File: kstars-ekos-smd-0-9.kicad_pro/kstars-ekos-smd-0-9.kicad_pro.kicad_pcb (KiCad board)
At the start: 2 copper layers, 86.5 x 56.5 mm, 36 parts, among them J1 Raspberry_Pi_2_3, J2 Conn_01x04, J3 Conn_01x04, U1 AP64501SP-13, U2 TLP3553ATP1_F, U3 TLP3553ATP1_F, U4 TLP3553ATP1_F, U5 TLP3553ATP1_F, U6 TLP241ATP1_F, U7 TLP241ATP1_F

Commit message: Final design submitted to fab.
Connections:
- H5 pad 1: Net-(H5-Pad1) -> GND
- H5 pad 2: GND -> Net-(H5-Pad2)
- U5 pad 4: Net-(H5-Pad1) -> Net-(H5-Pad2)
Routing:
- net Net-(H5-Pad1): track 5.57 -> 0.00 mm, vias 1 -> 0
- net Net-(H5-Pad2): track 0.00 -> 5.45 mm, vias 0 -> 1
- net Net-(C13-Positive): track 32.1 -> 32.9 mm
- net GND: vias 97 -> 98
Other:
- outline, holes or cut-outs redrawn

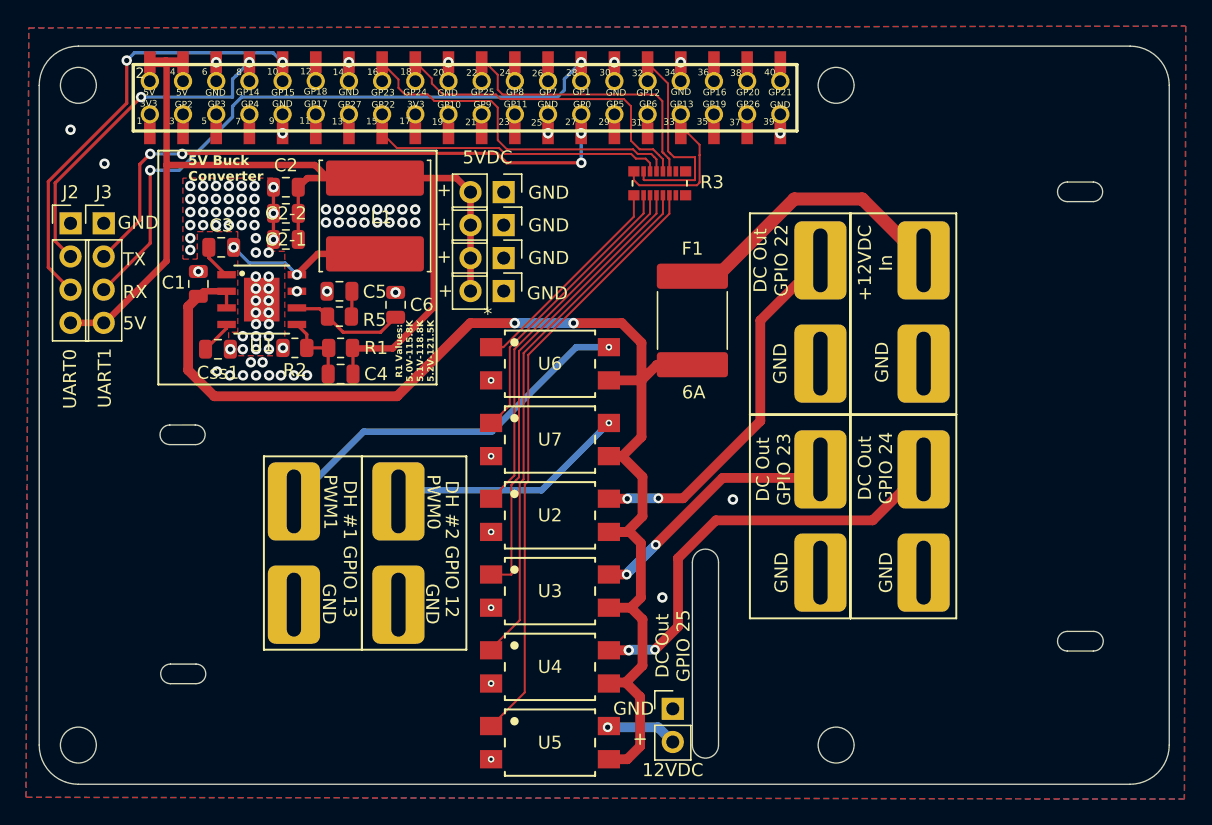
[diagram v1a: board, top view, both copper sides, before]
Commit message: Corrected hole locations.  Final upload to fab.
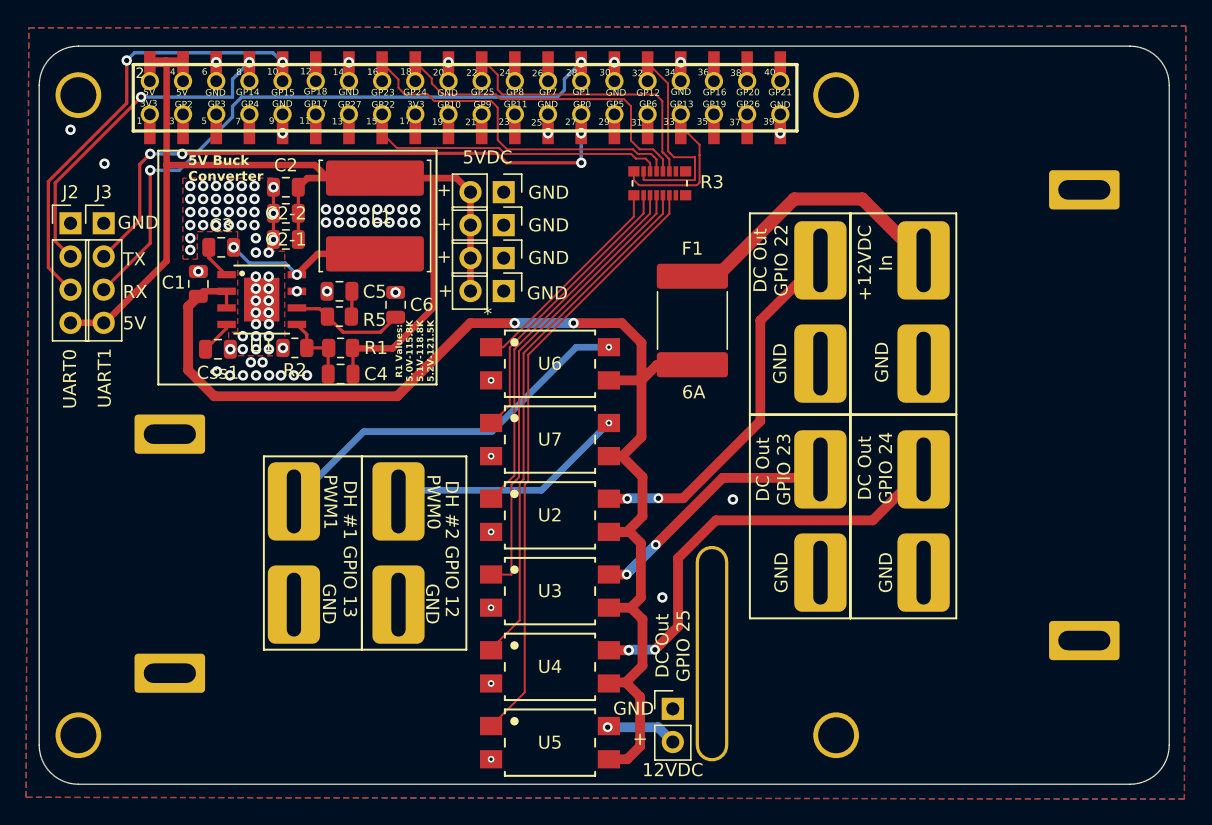
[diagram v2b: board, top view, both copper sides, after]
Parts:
- added REF**: MountingHole_2.75mm_Pad, Mounting_Holes:MountingHole_2.75mm_Pad, F.Cu at (143.0, 79.2)
- added REF**: MountingHole_2.75mm_Pad, Mounting_Holes:MountingHole_2.75mm_Pad, F.Cu at (201.0, 128.2)
- added REF**: Zip_Tie_Hole_1.5mm_2mm_Pad, Mounting_Holes:Zip_Tie_Hole_1.5mm_2mm_Pad, F.Cu at (220.0, 121.0)
- added REF**: Zip_Tie_Hole_1.5mm_2mm_Pad, Mounting_Holes:Zip_Tie_Hole_1.5mm_2mm_Pad, F.Cu at (220.0, 86.5)
- added REF**: Zip_Tie_Hole_1.5mm_2mm_Pad, Mounting_Holes:Zip_Tie_Hole_1.5mm_2mm_Pad, F.Cu at (150.0, 123.5)
- added REF**: Camera_Cable_Hole_2mm_16mm_Pad, Mounting_Holes:Camera_Cable_Hole_2mm_16mm_Pad, F.Cu at (191.5, 122.0)
- added REF**: MountingHole_2.75mm_Pad, Mounting_Holes:MountingHole_2.75mm_Pad, F.Cu at (201.0, 79.2)
- added REF**: Zip_Tie_Hole_1.5mm_2mm_Pad, Mounting_Holes:Zip_Tie_Hole_1.5mm_2mm_Pad, F.Cu at (150.0, 105.2)
- added REF**: MountingHole_2.75mm_Pad, Mounting_Holes:MountingHole_2.75mm_Pad, F.Cu at (143.0, 128.2)
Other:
- outline, holes or cut-outs redrawn

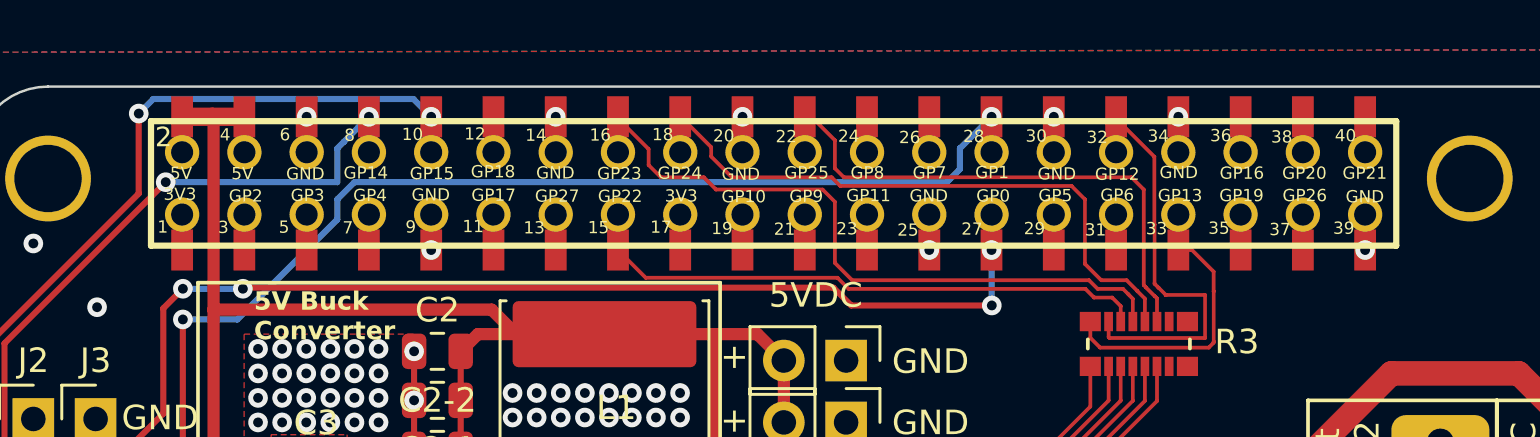
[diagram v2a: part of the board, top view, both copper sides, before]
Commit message: Updated 40-pin numbering silkscreen.
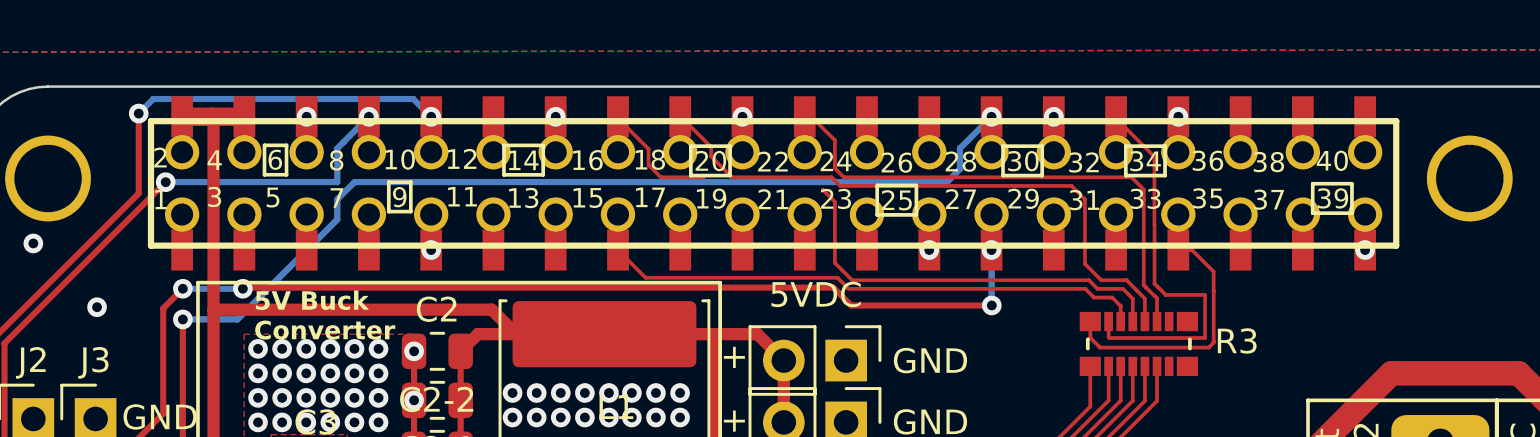
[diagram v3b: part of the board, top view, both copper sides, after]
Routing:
- net DC_2: track 26.8 -> 21.7 mm

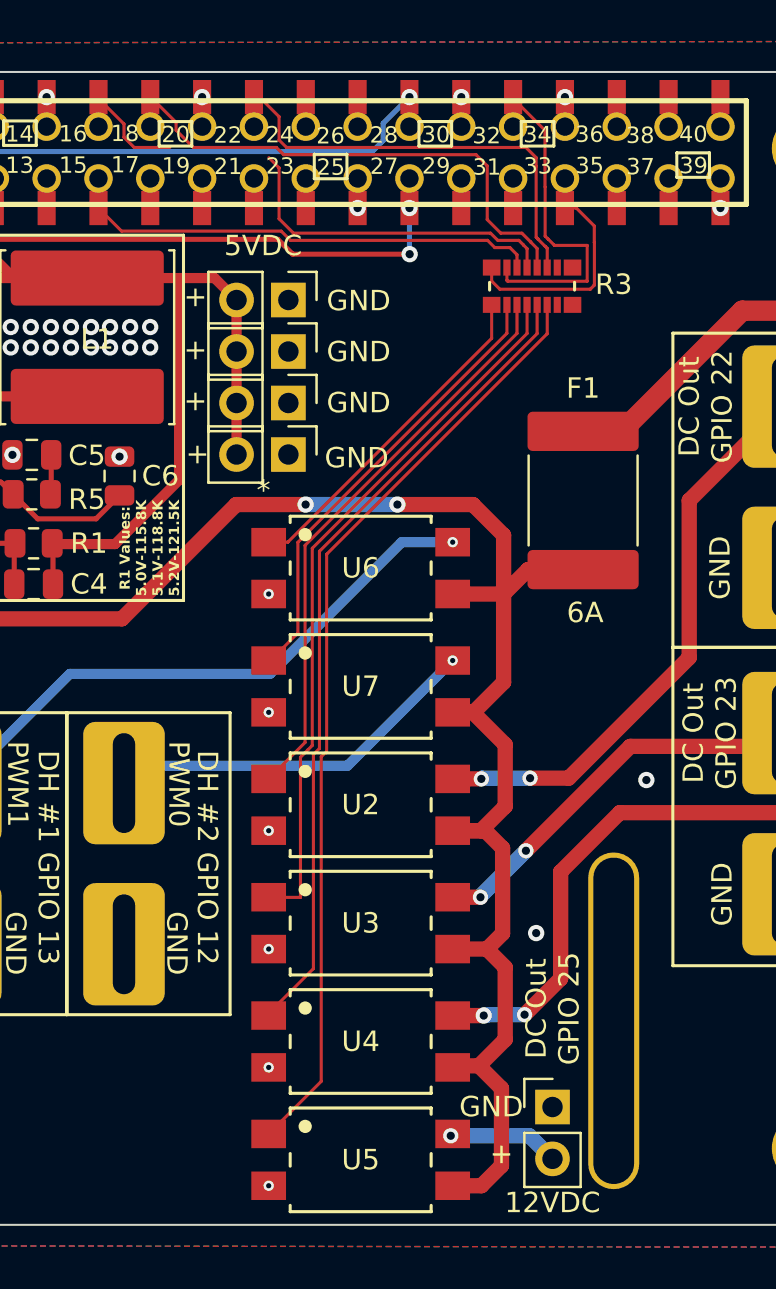
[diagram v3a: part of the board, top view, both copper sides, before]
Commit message: Fixed GPIO16 trace . .
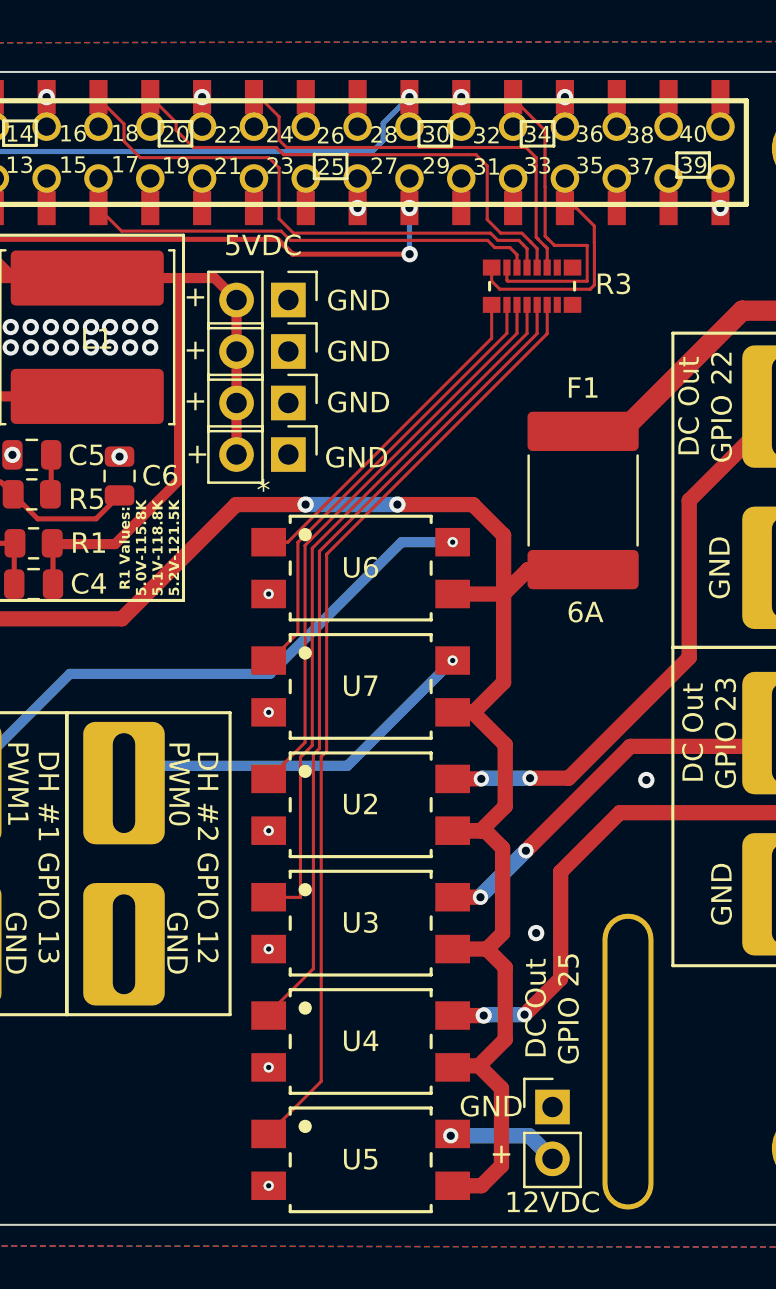
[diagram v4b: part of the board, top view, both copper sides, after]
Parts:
- moved REF** 2.12 mm to (192.2, 124.0)
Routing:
- net DC_2: track 21.7 -> 26.9 mm
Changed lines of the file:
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@@
 	(footprint "Mounting_Holes:Camera_Cable_Hole_2mm_16mm_Pad"
 		(layer "F.Cu")
-		(at 191.5 122 90)
+		(at 192.2 124 90)
 		(descr "Mounting Hole 2.7mm, generated by kicad-footprint-generator mountinghole.py")
 		(tags "mountinghole")
@@
 		(pad "1" thru_hole oval
 			(at 0 0 90)
-			(size 16.5 2.5)
-			(drill oval 16 2)
+			(size 14.5 2.5)
+			(drill oval 14 2)
 			(layers "*.Cu" "*.Mask")
 			(remove_unused_layers yes)
@@
 	)
 	(segment
-		(start 185.9651 83.4)
-		(end 187 83.4)
+		(start 184.7534 79.5534)
+		(end 185.3 80.1)
 		(width 0.1524)
 		(layer "F.Cu")
@@
 	)
 	(segment
-		(start 175.319617 79.5534)
-		(end 184.7534 79.5534)
+		(start 187.43321 83.838058)
+		(end 187.746634 84.15148)
 		(width 0.1524)
 		(layer "F.Cu")
@@
 	)
 	(segment
-		(start 187.43321 83.83321)
-		(end 187.43321 83.838058)
+		(start 187.746634 84.15148)
+		(end 187.746634 85.0856)
 		(width 0.1524)
 		(layer "F.Cu")
@@
 	)
 	(segment
-		(start 168.78935 76.708)
-		(end 170.053 77.97165)
+		(start 187.43321 83.83321)
+		(end 187.43321 83.838058)
 		(width 0.1524)
 		(layer "F.Cu")
@@
 	)
 	(segment
-		(start 187.43321 83.838058)
-		(end 187.746634 84.15148)
+		(start 170.9 79.2)
+		(end 174.966216 79.2)
 		(width 0.1524)
 		(layer "F.Cu")
@@
 	)
 	(segment
-		(start 187.746634 84.15148)
-		(end 187.746634 85.0856)
+		(start 185.3 80.1)
+		(end 185.3 82.7349)
 		(width 0.1524)
 		(layer "F.Cu")
@@
 	)
 	(segment
-		(start 185.3 82.7349)
-		(end 185.9651 83.4)
+		(start 187 83.4)
+		(end 187.43321 83.83321)
 		(width 0.1524)
 		(layer "F.Cu")
@@
 	(segment
 		(start 174.966216 79.2)
-		(end 175.319617 79.5534)
+		(end 175.319616 79.5534)
 		(width 0.1524)
 		(layer "F.Cu")
@@
 	)
 	(segment
-		(start 170.053 78.353)
-		(end 170.9 79.2)
+		(start 175.319616 79.5534)
+		(end 184.7534 79.5534)
 		(width 0.1524)
 		(layer "F.Cu")
@@
 	)
 	(segment
-		(start 184.7534 79.5534)
-		(end 185.3 80.1)
+		(start 185.3 82.7349)
+		(end 185.9651 83.4)
 		(width 0.1524)
 		(layer "F.Cu")
@@
 	)
 	(segment
-		(start 185.3 80.1)
-		(end 185.3 82.7349)
+		(start 170.053 77.97165)
+		(end 170.053 78.353)
 		(width 0.1524)
 		(layer "F.Cu")
@@
 	)
 	(segment
-		(start 187 83.4)
-		(end 187.43321 83.83321)
+		(start 185.9651 83.4)
+		(end 187 83.4)
 		(width 0.1524)
 		(layer "F.Cu")
@@
 	)
 	(segment
-		(start 170.9 79.2)
-		(end 174.966216 79.2)
+		(start 168.78935 76.708)
+		(end 170.053 77.97165)
 		(width 0.1524)
 		(layer "F.Cu")
@@
 	)
 	(segment
-		(start 170.053 77.97165)
-		(end 170.053 78.353)
+		(start 170.053 78.353)
+		(end 170.9 79.2)
 		(width 0.1524)
 		(layer "F.Cu")
@@
 	)
 	(segment
-		(start 187.07981 83.979594)
-		(end 187.07981 83.984442)
+		(start 174.6 79.7)
+		(end 175.1 80.2)
 		(width 0.1524)
 		(layer "F.Cu")
@@
 	)
 	(segment
-		(start 166.284056 76.8335)
-		(end 167.5 78.049444)
+		(start 175.8051 83.4)
+		(end 185.465316 83.4)
 		(width 0.1524)
 		(layer "F.Cu")
@@
 	)
 	(segment
-		(start 175.8051 83.4)
-		(end 185.465316 83.4)
+		(start 185.818717 83.7534)
+		(end 186.853616 83.7534)
 		(width 0.1524)
 		(layer "F.Cu")
@@
 	)
 	(segment
-		(start 187.07981 83.984442)
-		(end 187.253112 84.157743)
+		(start 175.1 82.6949)
+		(end 175.8051 83.4)
 		(width 0.1524)
 		(layer "F.Cu")
@@
 	)
 	(segment
-		(start 185.818717 83.7534)
-		(end 186.853616 83.7534)
+		(start 166.284056 76.8335)
+		(end 167.5 78.049444)
 		(width 0.1524)
 		(layer "F.Cu")
@@
 	)
 	(segment
-		(start 174.6 79.7)
-		(end 175.1 80.2)
+		(start 167.5 78.049444)
+		(end 167.5 78.9)
 		(width 0.1524)
 		(layer "F.Cu")
@@
 	)
 	(segment
-		(start 185.465316 83.4)
-		(end 185.818717 83.7534)
+		(start 168.3 79.7)
+		(end 174.6 79.7)
 		(width 0.1524)
 		(layer "F.Cu")
@@
 	)
 	(segment
-		(start 168 79.2)
-		(end 169.751 79.2)
+		(start 186.853616 83.7534)
+		(end 187.07981 83.979594)
 		(width 0.1524)
 		(layer "F.Cu")
@@
 	)
 	(segment
-		(start 167.5 78.049444)
-		(end 167.5 78.7)
+		(start 167.5 78.9)
+		(end 168.3 79.7)
 		(width 0.1524)
 		(layer "F.Cu")
@@
 	)
 	(segment
-		(start 167.5 78.7)
-		(end 168 79.2)
+		(start 187.07981 83.979594)
+		(end 187.07981 83.984442)
 		(width 0.1524)
 		(layer "F.Cu")
@@
 	)
 	(segment
-		(start 175.1 82.6949)
-		(end 175.8051 83.4)
+		(start 185.465316 83.4)
+		(end 185.818717 83.7534)
 		(width 0.1524)
 		(layer "F.Cu")
@@
 	)
 	(segment
-		(start 186.853616 83.7534)
-		(end 187.07981 83.979594)
+		(start 175.1 80.2)
+		(end 175.1 82.6949)
 		(width 0.1524)
 		(layer "F.Cu")
@@
 	)
 	(segment
-		(start 175.1 80.2)
-		(end 175.1 82.6949)
+		(start 187.07981 83.984442)
+		(end 187.253112 84.157743)
 		(width 0.1524)
 		(layer "F.Cu")
